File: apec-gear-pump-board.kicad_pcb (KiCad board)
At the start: 2 copper layers, 44.5 x 29.5 mm, 11 parts, among them J1 Screw_Terminal_01x06, J2 Screw_Terminal_01x02, J3 Screw_Terminal_01x04

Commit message: Fixed mistake
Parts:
- moved C1 7.71 mm to (57.9, 84.5)
- moved R1 3.86 mm to (49.6, 84.5)
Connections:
- C1 pad 1: Net-(J3-SPEED_IN) -> Net-(J1-SPEED_IN)
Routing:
- net Net-(J1-SPEED_IN): track 6.42 -> 10.4 mm
- net Net-(J3-SPEED_IN): track 8.94 -> 5.07 mm
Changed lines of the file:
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@@
   )
   (footprint "Resistor_THT:R_Axial_DIN0204_L3.6mm_D1.6mm_P5.08mm_Horizontal" (layer "F.Cu")
-    (at 53.425 84.525)
+    (at 49.57 84.475)
     (descr "Resistor, Axial_DIN0204 series, Axial, Horizontal, pin pitch=5.08mm, 0.167W, length*diameter=3.6*1.6mm^2, http://cdn-reichelt.de/documents/datenblatt/B400/1_4W%23YAG.pdf")
     (tags "Resistor Axial_DIN0204 series Axial Horizontal pin pitch 5.08mm 0.167W length 3.6mm diameter 1.6mm")
@@
   )
   (footprint "Capacitor_THT:C_Rect_L4.6mm_W3.0mm_P2.50mm_MKS02_FKP02" (layer "F.Cu")
-    (at 50.225 84.525 -90)
+    (at 57.935 84.525 -90)
     (descr "C, Rect series, Radial, pin pitch=2.50mm, , length*width=4.6*3.0mm^2, Capacitor, http://www.wima.de/DE/WIMA_MKS_02.pdf")
     (tags "C Rect series Radial pin pitch 2.50mm  length 4.6mm width 3.0mm Capacitor")
@@
       (stroke (width 0.1) (type solid)) (layer "F.Fab"))
     (pad "1" thru_hole circle (at 0 0 270) (size 1.4 1.4) (drill 0.7) (layers "*.Cu" "*.Mask")
-      (net 1 "Net-(J3-SPEED_IN)") (pintype "passive"))
+      (net 5 "Net-(J1-SPEED_IN)") (pintype "passive"))
     (pad "2" thru_hole circle (at 2.5 0 270) (size 1.4 1.4) (drill 0.7) (layers "*.Cu" "*.Mask")
       (net 2 "Net-(J1-SIGNAL_GND)") (pintype "passive"))
@@
     (style (thickness 0.1) (arrow_length 1.27) (text_position_mode 0) (extension_height 0.58642) (extension_offset 0.5) keep_text_aligned)
   )
-  (segment (start 44.5 84.48) (end 50.18 84.48) (width 1) (layer "F.Cu") (net 1))
-  (segment (start 50.225 84.525) (end 53.425 84.525) (width 1) (layer "F.Cu") (net 1))
-  (segment (start 50.18 84.48) (end 50.225 84.525) (width 1) (layer "F.Cu") (net 1))
+  (segment (start 49.57 84.475) (end 44.505 84.475) (width 1) (layer "F.Cu") (net 1))
+  (segment (start 44.505 84.475) (end 44.5 84.48) (width 1) (layer "F.Cu") (net 1))
   (segment (start 44.5 87.02) (end 50.22 87.02) (width 1) (layer "F.Cu") (net 2))
   (segment (start 50.22 87.02) (end 50.225 87.025) (width 1) (layer "F.Cu") (net 2))
@@
   (segment (start 58.255 81.935) (end 52.17 75.85) (width 1) (layer "F.Cu") (net 4))
   (segment (start 64.9 81.935) (end 58.255 81.935) (width 1) (layer "F.Cu") (net 4))
+  (segment (start 57.935 84.525) (end 54.7 84.525) (width 1) (layer "F.Cu") (net 5))
   (segment (start 64.85 84.525) (end 64.9 84.475) (width 1) (layer "F.Cu") (net 5))
-  (segment (start 58.505 84.525) (end 64.85 84.525) (width 1) (layer "F.Cu") (net 5))
+  (segment (start 54.7 84.525) (end 54.65 84.475) (width 1) (layer "F.Cu") (net 5))
+  (segment (start 64.9 84.475) (end 57.985 84.475) (width 1) (layer "F.Cu") (net 5))
+  (segment (start 57.985 84.475) (end 57.935 84.525) (width 1) (layer "F.Cu") (net 5))
   (segment (start 64.895 89.56) (end 64.9 89.555) (width 1) (layer "F.Cu") (net 6))
   (segment (start 44.5 89.56) (end 64.895 89.56) (width 1) (layer "F.Cu") (net 6))

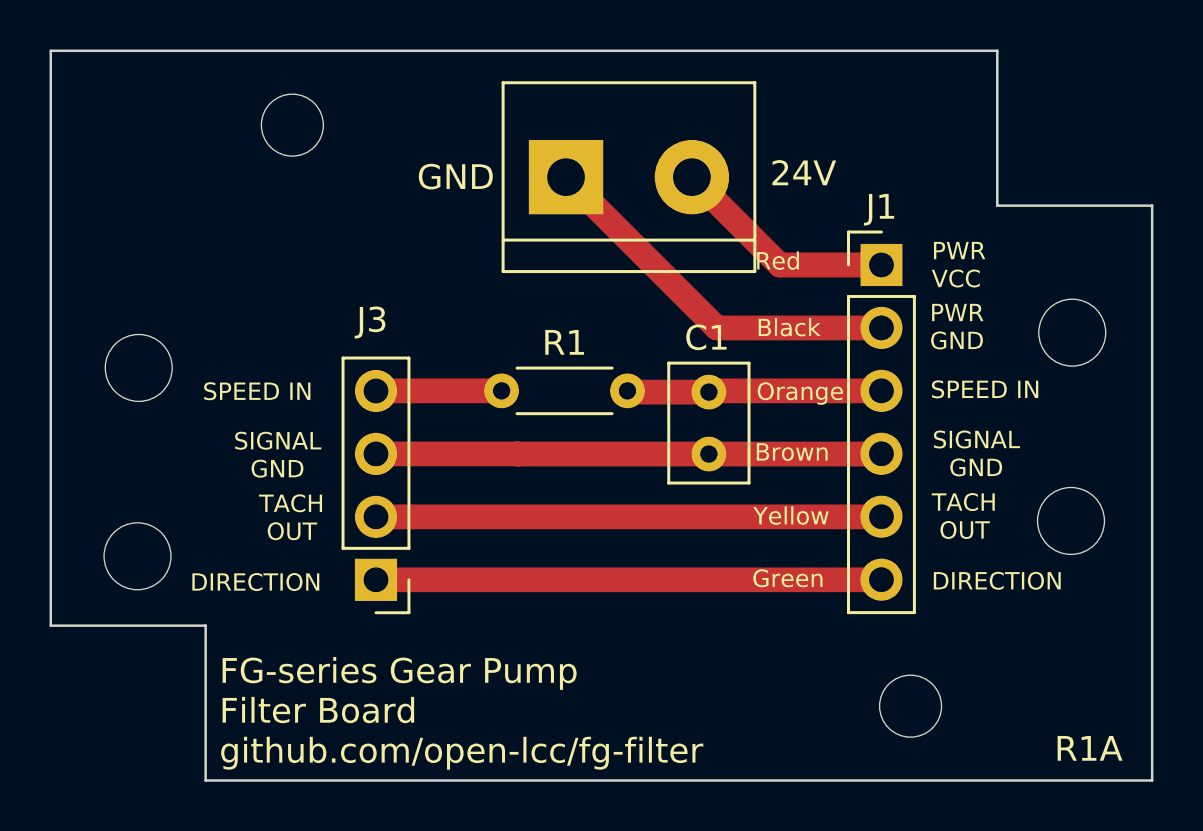
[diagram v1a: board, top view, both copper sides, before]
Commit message: Cleaned stuff up, and switched to wider tracks for Power
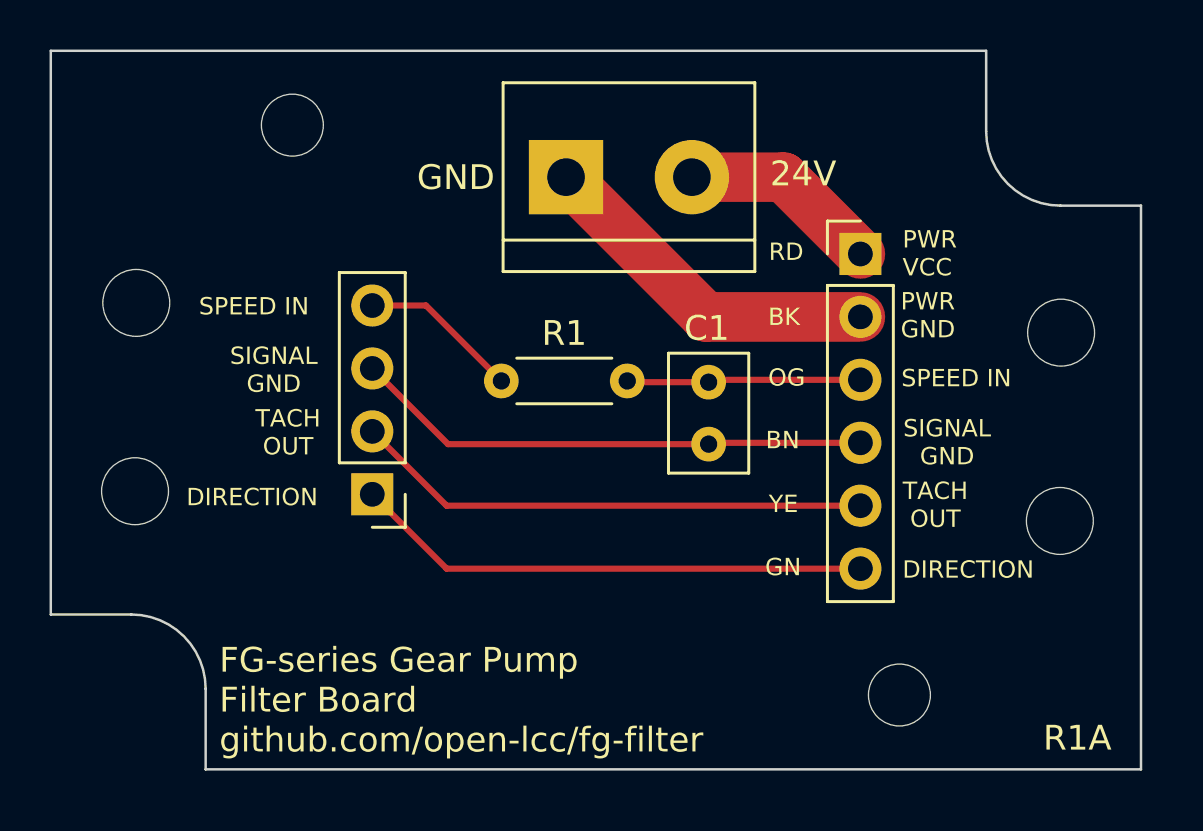
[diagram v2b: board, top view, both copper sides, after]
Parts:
- moved J3 3.45 mm to (44.4, 88.7)
- moved REF** 2.63 mm to (34.8, 88.5)
- moved REF** 2.63 mm to (34.8, 80.9)
- moved J1 0.96 mm to (64.0, 79.0)
- moved H2 0.64 mm to (65.6, 96.8)
- moved REF** 0.45 mm to (72.1, 89.7)
- moved REF** 0.45 mm to (72.2, 82.1)
- moved C1 0.40 mm to (57.9, 84.1)
- moved R1 0.40 mm to (49.6, 84.1)
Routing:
- net Net-(J3-SPEED_IN): track 5.07 -> 6.47 mm
- net Net-(J1-PWR_GND): track 15.3 -> 14.2 mm
- net Net-(J1-PWR_VCC): track 9.12 -> 8.08 mm
- net Net-(J1-SPEED_IN): track 10.4 -> 9.47 mm
- net Net-(J1-SIGNAL_GND): track 20.4 -> 21.0 mm
- net Net-(J1-TACHO_OUT): track 20.4 -> 20.9 mm
- net Net-(J1-DIRECTION): track 20.4 -> 20.9 mm
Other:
- board size 44.5 x 29.5 mm -> 44 x 29 mm
- board text added: "BK"
- board text added: "BN"
- board text added: "GN"
- board text added: "Hammond 1551GBK"
- board text added: "OG"
- board text added: "RD"
- board text added: "YE"
- board text removed: "Black"
- board text removed: "Brown"
- board text removed: "Green"
- board text removed: "Hammond 1551F"
- board text removed: "Orange"
- board text removed: "Red"
- board text removed: "Yellow"

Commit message: Updated the board to do level shifting
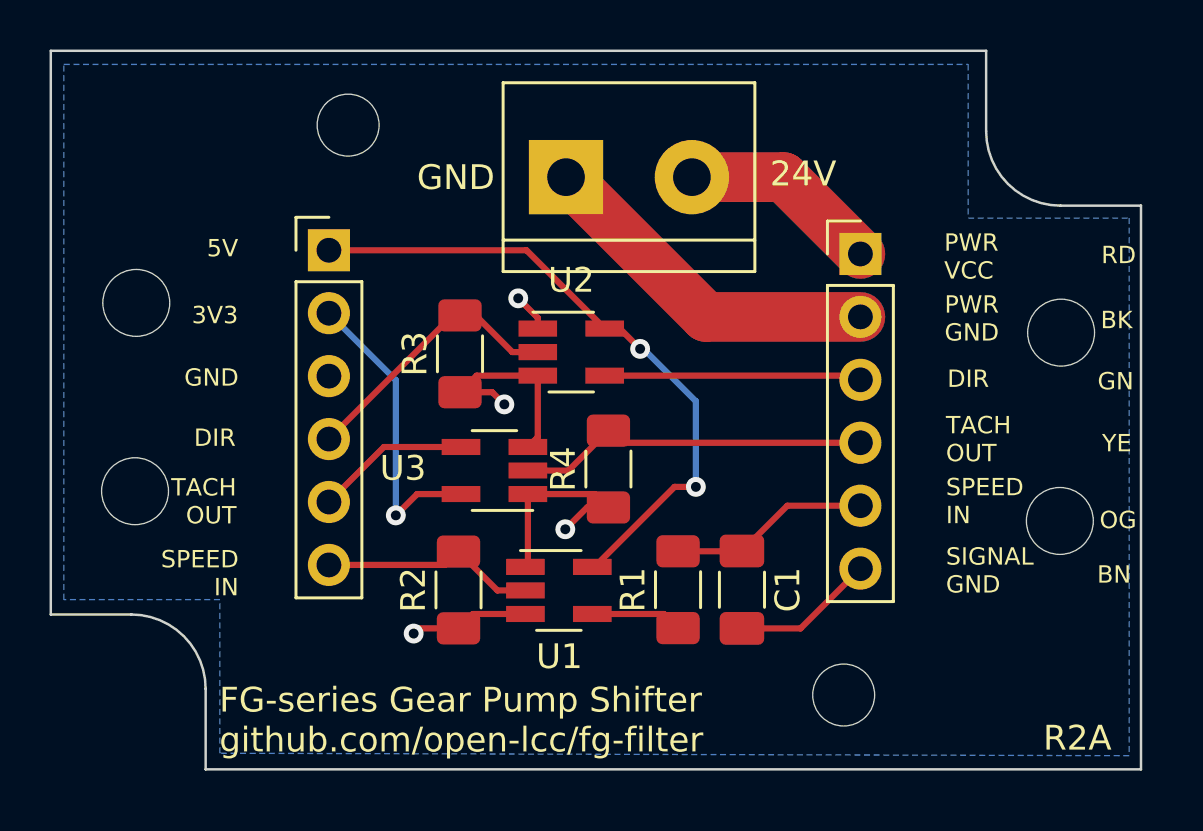
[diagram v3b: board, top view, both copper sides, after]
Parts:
- removed J3: Screw_Terminal_01x04, Connector_PinHeader_2.54mm:PinHeader_1x04_P2.54mm_Vertical
- added J4: Screw_Terminal_01x06, Connector_PinHeader_2.54mm:PinHeader_1x06_P2.54mm_Vertical, F.Cu at (42.6, 78.8)
- added R2: 10K, Resistor_SMD:R_1206_3216Metric_Pad1.30x1.75mm_HandSolder, F.Cu at (47.8, 92.5)
- added R3: 10K, Resistor_SMD:R_1206_3216Metric_Pad1.30x1.75mm_HandSolder, F.Cu at (47.9, 83.0)
- added R4: 10K, Resistor_SMD:R_1206_3216Metric_Pad1.30x1.75mm_HandSolder, F.Cu at (53.9, 87.6)
- added U1: 74LV1T125, Package_TO_SOT_SMD:SOT-23-5_HandSoldering, F.Cu at (51.9, 92.5)
- added U2: 74LV1T125, Package_TO_SOT_SMD:SOT-23-5_HandSoldering, F.Cu at (52.4, 82.9)
- added U3: 74LV1T125, Package_TO_SOT_SMD:SOT-23-5_HandSoldering, F.Cu at (49.3, 87.7)
- C1: value C_Small -> 10 nF; footprint Capacitor_THT:C_Rect_L4.6mm_W3.0mm_P2.50mm_MKS02_FKP02 -> Capacitor_SMD:C_1206_3216Metric_Pad1.33x1.80mm_HandSolder
- R1: value R_Small -> 51K; footprint Resistor_THT:R_Axial_DIN0204_L3.6mm_D1.6mm_P5.08mm_Horizontal -> Resistor_SMD:R_1206_3216Metric_Pad1.30x1.75mm_HandSolder
- moved R1 11.0 mm to (56.7, 92.5), turned to 90 degrees
- moved C1 8.48 mm to (59.3, 92.5)
- moved H1 2.25 mm to (43.4, 73.8)
- moved H2 2.25 mm to (63.4, 96.8)
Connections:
- C1 pad 1: Net-(J1-SPEED_IN) -> SPEED_IN_5V
- C1 pad 2: Net-(J1-SIGNAL_GND) -> GND
- J1 pad 3: Net-(J1-SPEED_IN) -> DIRECTION_5V
- J1 pad 4: Net-(J1-SIGNAL_GND) -> TACHO_OUT_5V
- J1 pad 5: Net-(J1-TACHO_OUT) -> SPEED_IN_5V
- J1 pad 6: Net-(J1-DIRECTION) -> GND
- R1 pad 2: Net-(J1-SPEED_IN) -> SPEED_IN_5V
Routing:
- net GND: track 0.00 -> 29.2 mm, vias 0 -> 4
- net +5V: track 0.00 -> 26.3 mm, vias 0 -> 2
- net Net-(J1-SIGNAL_GND): track 21.0 -> 0.00 mm
- net Net-(J1-TACHO_OUT): track 20.9 -> 0.00 mm
- net Net-(J1-DIRECTION): track 20.9 -> 0.00 mm
- net TACHO_OUT_5V: track 0.00 -> 14.3 mm
- net Net-(J1-PWR_GND): track 14.2 -> 28.4 mm
- net +3V3: track 0.00 -> 12.3 mm, vias 0 -> 1
- net DIRECTION_3V3: track 0.00 -> 11.1 mm
- net DIRECTION_5V: track 0.00 -> 10.4 mm
- net Net-(J1-SPEED_IN): track 9.47 -> 0.00 mm
- net SPEED_IN_3V3: track 0.00 -> 8.80 mm
- net SPEED_IN_5V: track 0.00 -> 8.12 mm
- net Net-(J1-PWR_VCC): track 8.08 -> 16.2 mm
- net TACHO_OUT_3V3: track 0.00 -> 6.25 mm
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- added copper zone on B.Cu, net GND
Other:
- board text added: "3V3"
- board text added: "5V"
- board text added: "DIR"
- board text added: "FG-series Gear Pump Shifter github.com/open-lcc/fg-filter"
- board text added: "R2A"
- board text removed: "DIRECTION"
- board text removed: "FG-series Gear Pump Filter Board github.com/open-lcc/fg-filter"
- board text removed: "R1A"

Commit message: Added decoupling caps and Variegated Coffee logo
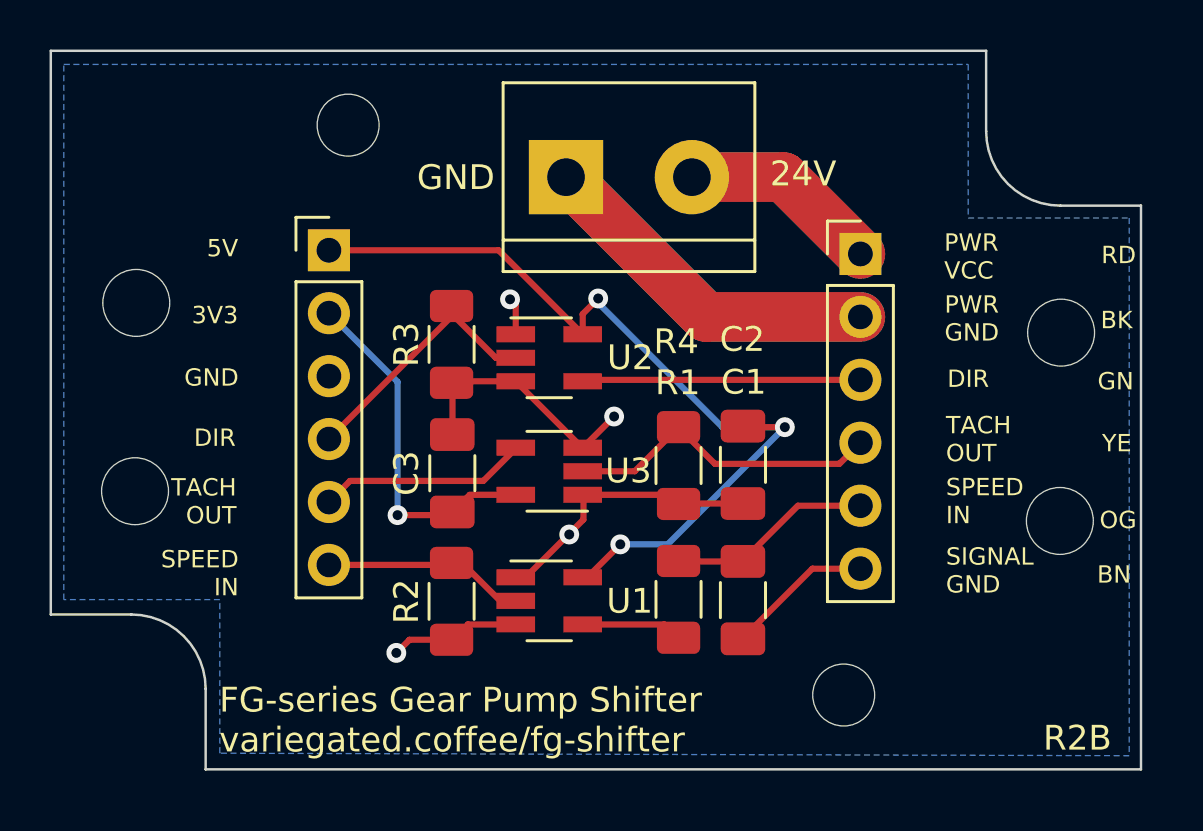
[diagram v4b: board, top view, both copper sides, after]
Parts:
- added C2: 1 uF, Capacitor_SMD:C_1206_3216Metric_Pad1.33x1.80mm_HandSolder, F.Cu at (59.3, 87.5)
- added C3: 1 uF, Capacitor_SMD:C_1206_3216Metric_Pad1.33x1.80mm_HandSolder, F.Cu at (47.6, 87.8)
- added REF**: OSHW-Logo2_9.8x8mm_SilkScreen, Symbol:OSHW-Logo2_9.8x8mm_SilkScreen, B.Cu at (58.0, 87.4)
- added REF**: VariegatedCoffeeLogo_Small, Variegated:VariegatedCoffeeLogo_Small, B.Cu at (48.2, 92.9)
- moved R4 2.83 mm to (56.7, 87.5)
- moved U3 2.21 mm to (51.5, 87.7)
- moved U2 0.92 mm to (51.5, 83.1)
- moved U1 0.57 mm to (51.5, 93.0)
- moved R2 0.54 mm to (47.5, 93.0)
- moved R3 0.51 mm to (47.5, 82.6)
- moved C1 0.42 mm to (59.3, 92.9)
- moved R1 0.39 mm to (56.7, 92.9)
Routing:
- net +5V: track 26.3 -> 35.2 mm, vias 2 -> 3
- net GND: track 29.2 -> 34.4 mm
- net TACHO_OUT_3V3: track 6.25 -> 8.48 mm
- net +3V3: track 12.3 -> 14.4 mm
- net TACHO_OUT_5V: track 14.3 -> 12.9 mm
- net DIRECTION_5V: track 10.4 -> 11.2 mm
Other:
- board text added: "FG-series Gear Pump Shifter variegated.coffee/fg-shifter"
- board text added: "R2B"
- board text removed: "FG-series Gear Pump Shifter github.com/open-lcc/fg-filter"
- board text removed: "R2A"

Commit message: More silk screen on the back, changed pinout on the connectors, to put optional pins towards one edge
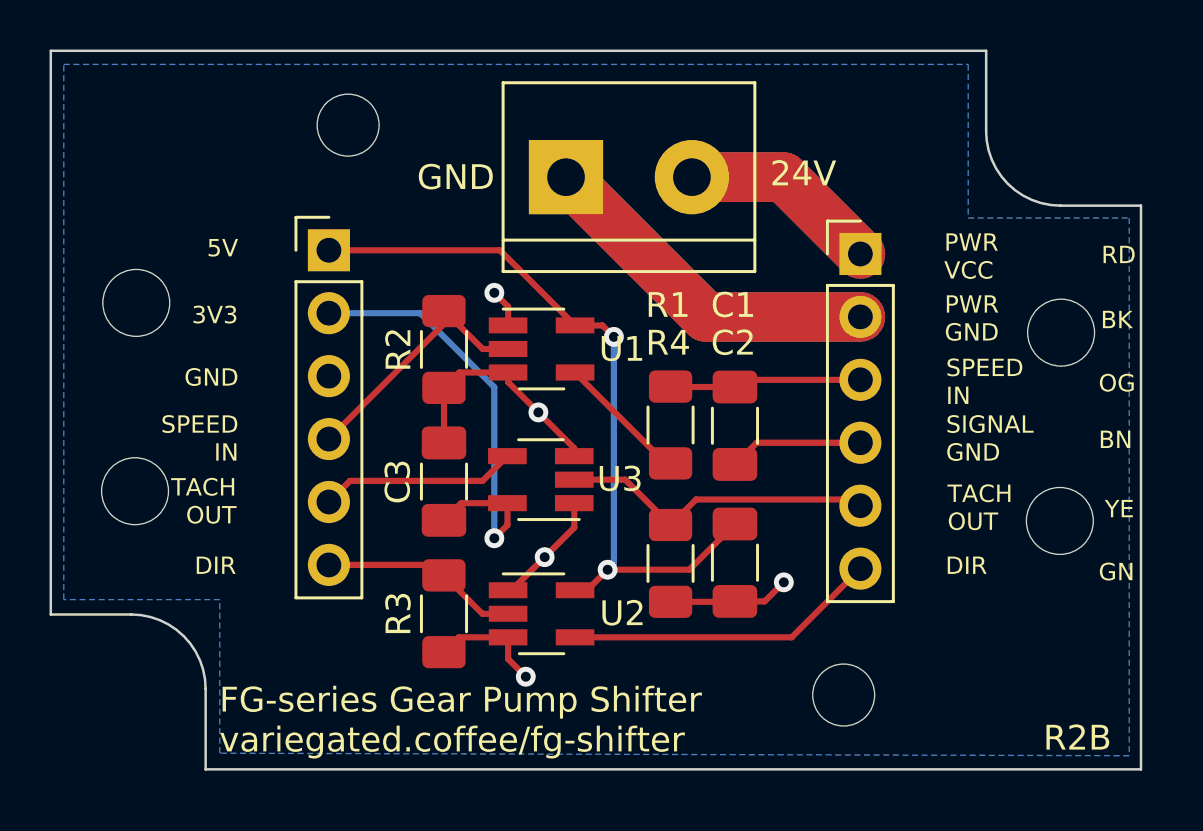
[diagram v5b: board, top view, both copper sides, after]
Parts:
- moved R3 10.9 mm to (47.2, 93.5)
- moved U2 10.3 mm to (51.2, 93.5)
- moved R2 10.2 mm to (47.2, 82.8)
- moved U1 10.2 mm to (51.2, 82.8)
- moved C1 7.05 mm to (59.0, 85.9)
- moved R1 7.05 mm to (56.4, 85.9)
- moved C2 3.96 mm to (59.0, 91.4)
- moved R4 3.96 mm to (56.4, 91.4)
- moved C3 0.48 mm to (47.2, 88.1)
- moved U3 0.48 mm to (51.2, 88.1)
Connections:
- J1 pad 3: DIRECTION_5V -> SPEED_IN_5V
- J1 pad 4: TACHO_OUT_5V -> GND
- J1 pad 5: SPEED_IN_5V -> TACHO_OUT_5V
- J1 pad 6: GND -> DIRECTION_5V
- J4 pad 4: DIRECTION_3V3 -> SPEED_IN_3V3
- J4 pad 6: SPEED_IN_3V3 -> DIRECTION_3V3
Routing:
- net +5V: track 35.2 -> 30.0 mm, vias 3 -> 2
- net +3V3: track 14.4 -> 18.5 mm
- net GND: track 34.4 -> 30.8 mm, vias 4 -> 5
- net DIRECTION_3V3: track 11.1 -> 8.05 mm
- net SPEED_IN_3V3: track 8.61 -> 10.3 mm
- net Net-(R1-Pad1): track 3.70 -> 5.37 mm
- net DIRECTION_5V: track 11.2 -> 12.7 mm
- net TACHO_OUT_3V3: track 8.48 -> 7.97 mm
